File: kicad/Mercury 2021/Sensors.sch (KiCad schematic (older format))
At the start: 10 parts

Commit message: Updated new board
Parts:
- added J16: Conn_01x16_Female, symbol Connector:Conn_01x16_Female
- added J17: Conn_01x06_Female, symbol Connector:Conn_01x06_Female
- added J18: Conn_01x02_Female, symbol Connector:Conn_01x02_Female
- added J19: Conn_01x09_Female, symbol Connector:Conn_01x09_Female
- added J20: Conn_01x08_Female, symbol Connector:Conn_01x08_Female
- added J21: Conn_01x04_Female, symbol Connector:Conn_01x04_Female
- U2, U3, U4, U5, U6, U7, U8, U9: renamed from U?; footprint Sensor_Distance:ST_VL53L1x -> Connector_PinHeader_2.54mm:PinHeader_1x06_P2.54mm_Vertical
- gave numbers to parts that had none: 2
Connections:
- net MP_A0: now reaches U10.1 (A0)
- net MP_A0: now also J21.1 (Pin_1)
- net MP_GND: now reaches U10.12 (GND)
- net MP_A1: now reaches U10.2 (A1)
- net MP_A1: now also J21.2 (Pin_2)
- net MP_A2: now reaches U10.21 (A2)
- net MP_A2: now also J21.3 (Pin_3)
- net MP_+5V: now reaches U10.24 (VCC)
- net MP_Reset: now reaches U10.3 (~RESET)
- net MP_Reset: now also J21.4 (Pin_4)
- net Arduino_Tx: now reaches A1.1 (TX1)
- net Arduino_Tx: now also J18.2 (Pin_2)
- net Arduino_D7: now reaches A1.10 (D7)
- net Arduino_D7: now also J19.4 (Pin_4)
- net Arduino_D8: now reaches A1.11 (D8)
- net Arduino_D8: now also J19.3 (Pin_3)
- net Arduino_D9: now reaches A1.12 (D9)
- net Arduino_D9: now also J19.2 (Pin_2)
- net Arduino_D10: now reaches A1.13 (D10)
- net Arduino_D10: now also J19.1 (Pin_1)
- net Arduino_3v3: now reaches A1.17 (3V3)
- net Arduino_3v3: now also J17.4 (Pin_4)
- net Arduino_AREF: now reaches A1.18 (AREF)
- net Arduino_AREF: now also J17.1 (Pin_1)
- net Arduino_A0: now reaches A1.19 (A0)
- net Arduino_A0: now also J20.1 (Pin_1)
- net Arduino_Rx: now reaches A1.2 (RX1)
- net Arduino_Rx: now also J18.1 (Pin_1)
- net Arduino_A1: now reaches A1.20 (A1)
- net Arduino_A1: now also J20.2 (Pin_2)
- net Arduino_A2: now reaches A1.21 (A2)
- net Arduino_A2: now also J20.3 (Pin_3)
- net Arduino_A3: now reaches A1.22 (A3)
- net Arduino_A3: now also J20.4 (Pin_4)
- net Arduino_A7: now reaches A1.25 (A6)
- net Arduino_A7: now also J20.7 (Pin_7)
- net Arduino_A8: now reaches A1.26 (A7)
- net Arduino_A8: now also J20.8 (Pin_8)
- net Arduino_5v: now reaches A1.27 (+5V)
- net Arduino_5v: now also J17.5 (Pin_5)
- net Arduino_GND: now reaches A1.29 (GND), A1.4 (GND)
- net Arduino_GND: now also J17.3 (Pin_3)
- net Arduino_Reset: now reaches A1.3 (~RESET)
- net Arduino_Reset: now also J17.6 (Pin_6)
- net Arduino_VIN: now reaches A1.30 (VIN)
- net Arduino_VIN: now also J17.2 (Pin_2)
- net Arduino_D2: now reaches A1.5 (D2)
- net Arduino_D2: now also J19.9 (Pin_9)
- net Arduino_D3: now reaches A1.6 (D3)
- net Arduino_D3: now also J19.8 (Pin_8)
- net Arduino_D4: now reaches A1.7 (D4)
- net Arduino_D4: now also J19.7 (Pin_7)
- net Arduino_D5: now reaches A1.8 (D5)
- net Arduino_D5: now also J19.6 (Pin_6)
- net Arduino_D6: now reaches A1.9 (D6)
- net Arduino_D6: now also J19.5 (Pin_5)
- net VDD0: now reaches U3.11 (AVDD)
- net GND0: now reaches U3.12 (GND), U3.3 (GND), U3.4 (GND), U3.6 (GND)
- net Sense0_XShut: now reaches U3.5 (XSHUT)
- net Sense0_XShut: now also J16.15 (Pin_15)
- net Sense0_GPIO: now reaches U3.7 (GPIO1)
- net Sense0_GPIO: now also J16.16 (Pin_16)
- net VDD1: now reaches U5.11 (AVDD)
- net GND1: now reaches U5.12 (GND), U5.3 (GND), U5.4 (GND), U5.6 (GND)
- net Sense1_XShut: now reaches U5.5 (XSHUT)
- net Sense1_XShut: now also J16.13 (Pin_13)
- net Sense1_GPIO: now reaches U5.7 (GPIO1)
- net Sense1_GPIO: now also J16.14 (Pin_14)
- net VDD2: now reaches U7.11 (AVDD)
- net GND2: now reaches U7.12 (GND), U7.3 (GND), U7.4 (GND), U7.6 (GND)
- net Sense2_XShut: now reaches U7.5 (XSHUT)
- net Sense2_XShut: now also J16.11 (Pin_11)
- net Sense2_GPIO: now reaches U7.7 (GPIO1)
- net Sense2_GPIO: now also J16.12 (Pin_12)
- net VDD3: now reaches U9.11 (AVDD)
- net GND3: now reaches U9.12 (GND), U9.3 (GND), U9.4 (GND), U9.6 (GND)
- net Sense3_XShut: now reaches U9.5 (XSHUT)
- net Sense3_XShut: now also J16.9 (Pin_9)
- net Sense3_GPIO: now reaches U9.7 (GPIO1)
- net Sense3_GPIO: now also J16.10 (Pin_10)
- net VDD8: now reaches U8.11 (AVDD)
- net GND8: now reaches U8.12 (GND), U8.3 (GND), U8.4 (GND), U8.6 (GND)
- net Sense7_XShut: now reaches U8.5 (XSHUT)
- net Sense7_XShut: now also J16.1 (Pin_1)
- net Sense7_GPIO: now reaches U8.7 (GPIO1)
- net Sense7_GPIO: now also J16.2 (Pin_2)
- net VDD7: now reaches U6.11 (AVDD)
- net GND7: now reaches U6.12 (GND), U6.3 (GND), U6.4 (GND), U6.6 (GND)
- net Sense6_XShut: now reaches U6.5 (XSHUT)
- net Sense6_XShut: now also J16.3 (Pin_3)
- net Sense6_GPIO: now reaches U6.7 (GPIO1)
- net Sense6_GPIO: now also J16.4 (Pin_4)
- net VDD6: now reaches U4.11 (AVDD)
- net GND6: now reaches U4.12 (GND), U4.3 (GND), U4.4 (GND), U4.6 (GND)
- net Sense5_XShut: now reaches U4.5 (XSHUT)
- net Sense5_XShut: now also J16.5 (Pin_5)
- net Sense5_GPIO: now reaches U4.7 (GPIO1)
- net Sense5_GPIO: now also J16.6 (Pin_6)
- net VDD5: now reaches U2.11 (AVDD)
- net GND5: now reaches U2.12 (GND), U2.3 (GND), U2.4 (GND), U2.6 (GND)
- net Sense4_XShut: now reaches U2.5 (XSHUT)
- net Sense4_XShut: now also J16.7 (Pin_7)
- net Sense4_GPIO: now reaches U2.7 (GPIO1)
- net Sense4_GPIO: now also J16.8 (Pin_8)
- new net NC: J20.5 (Pin_5), J20.6 (Pin_6)
- no-connect marks 30 -> 22
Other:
- moved on the sheet: A1

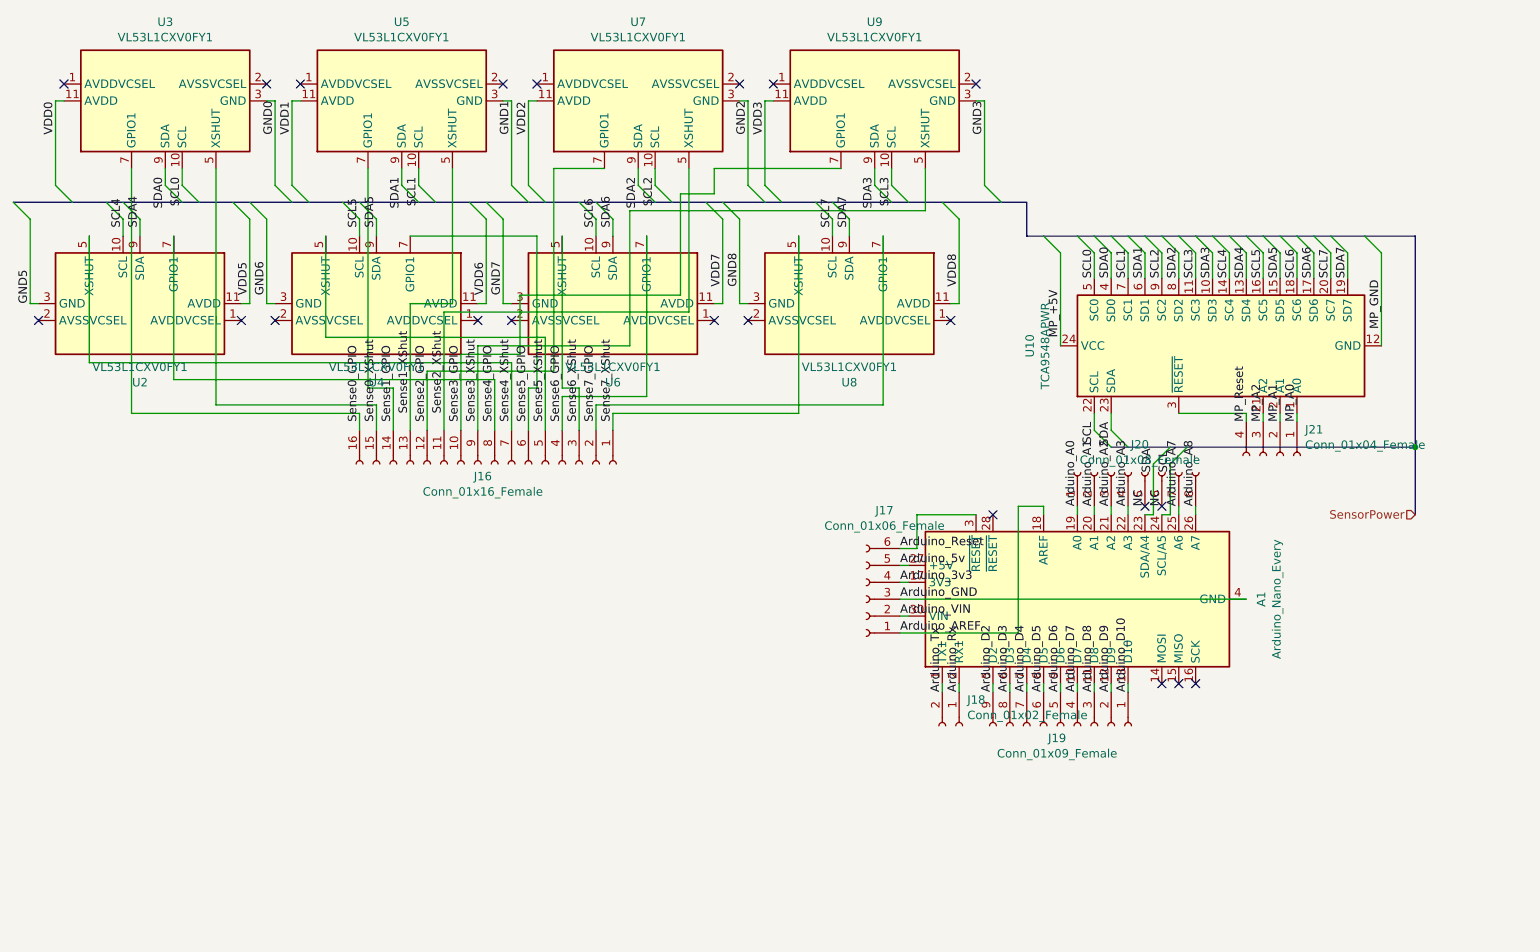
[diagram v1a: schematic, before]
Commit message: Updated the new PCB (lots of notes)
- added net
- changed symbols
- added footprints
- added ability to put the pi -> arduino cable through the board
- fixed global labels
- named connectors
- started adding things to title block

Notes:
- footprints for some parts were chosen at random, connectors need to be chosen on digikey
-- connectors for ribbon cables
-- USB connectors
-- screw terminals
- for these, the footprints may be wrong, so we need to make sure the connectors for them are spaced right
-- arduino
-- servo controller
-- PWM controller
- Board is unorganized, cluttered, and unusable, needs to be managed. considerations:
-- Pins carrying power and data should be separated by distance or GND
-- able to access connectors (not blocked by other things)
- Finish adding things to the title blocks and the PCB silkscreen
-- names or members
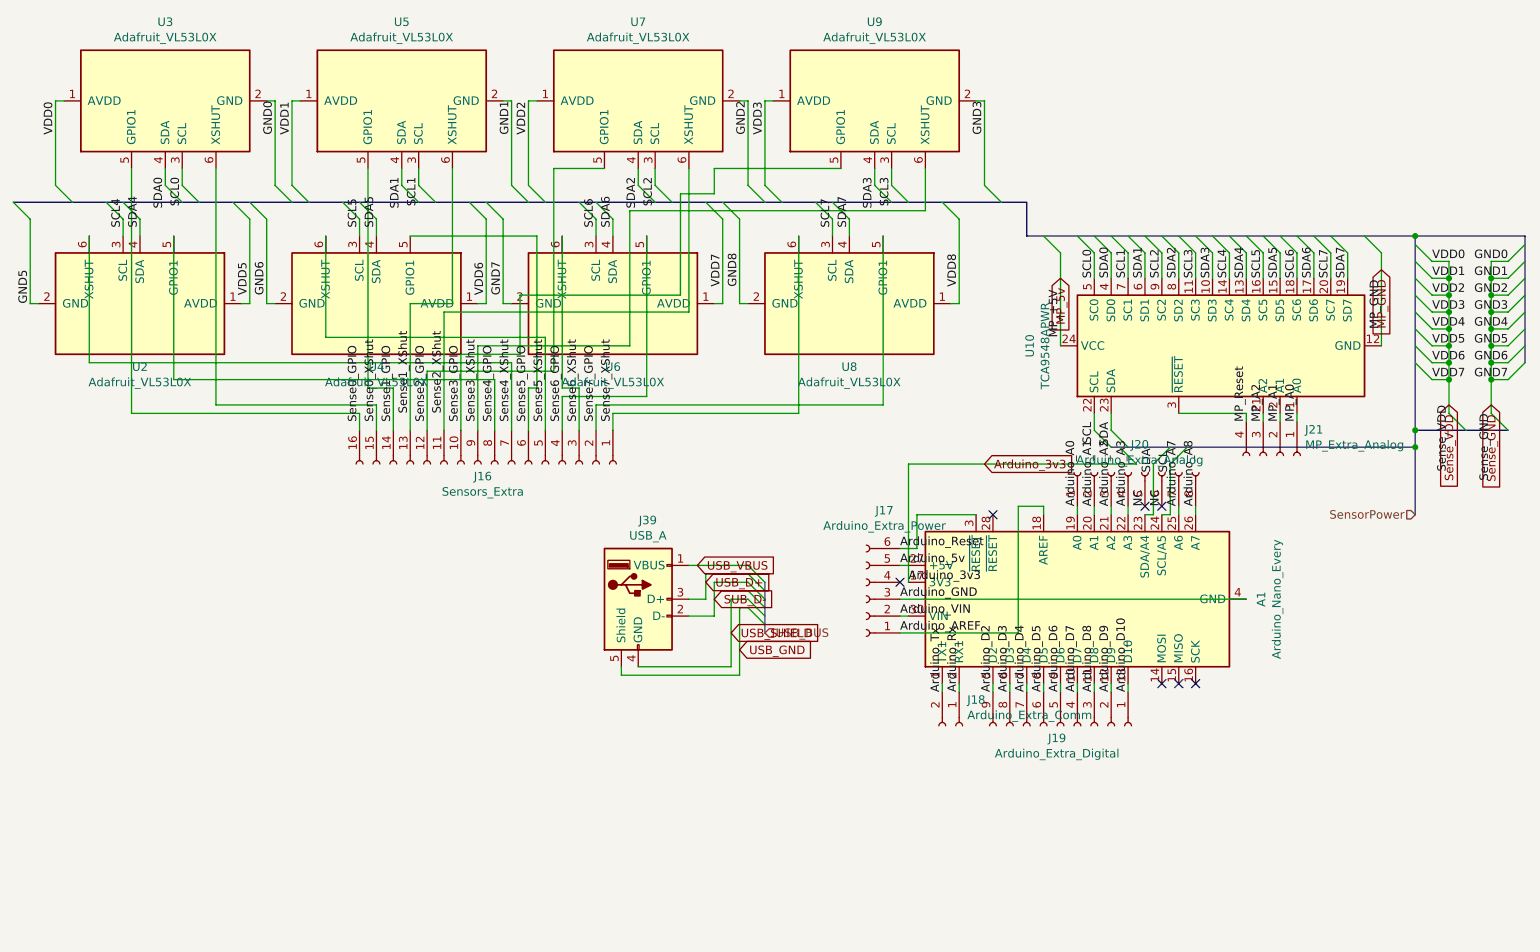
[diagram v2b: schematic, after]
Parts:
- removed U2, U3, U4, U5, U6, U7, U8, U9: VL53L1CXV0FY1, Connector_PinHeader_2.54mm:PinHeader_1x06_P2.54mm_Vertical, symbol Sensor_Distance:VL53L1CXV0FY1
- added J39: USB_A, Connector_USB:USB_A_Molex_105057_Vertical, symbol Connector:USB_A
- added U2, U3, U4, U5, U6, U7, U8, U9: Adafruit_VL53L0X, Mercury 2021:VL53L0X, symbol Sensor_Distance:Adafruit_VL53L0X
- A1: footprint Module:Arduino_Nano -> Module:Arduino_Nano_WithMountingHoles
- J16: value Conn_01x16_Female -> Sensors_Extra; footprint (none) -> Connector_PinSocket_2.54mm:PinSocket_1x16_P2.54mm_Vertical
- J17: value Conn_01x06_Female -> Arduino_Extra_Power; footprint (none) -> Connector_PinSocket_2.54mm:PinSocket_1x06_P2.54mm_Vertical
- J18: value Conn_01x02_Female -> Arduino_Extra_Comm; footprint (none) -> Connector_PinSocket_2.54mm:PinSocket_1x02_P2.54mm_Vertical
- J19: value Conn_01x09_Female -> Arduino_Extra_Digital; footprint (none) -> Connector_PinSocket_2.54mm:PinSocket_1x09_P2.54mm_Vertical
- J20: value Conn_01x08_Female -> Arduino_Extra_Analog; footprint (none) -> Connector_PinSocket_2.54mm:PinSocket_1x08_P2.54mm_Vertical
- J21: value Conn_01x04_Female -> MP_Extra_Analog; footprint (none) -> Connector_PinSocket_2.54mm:PinSocket_1x04_P2.54mm_Vertical
- U10: footprint Package_SO:TSSOP-24_4.4x7.8mm_P0.65mm -> Mercury 2021:TCA9548
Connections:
- net Arduino_3v3: no longer J17.4 (Pin_4)
- net GND8: now also U8.2 (GND)
- net SCL0: now also U3.3 (SCL)
- net SCL1: now also U5.3 (SCL)
- net SCL2: now also U7.3 (SCL)
- net SCL3: now also U9.3 (SCL)
- net SCL4: now also U2.3 (SCL)
- net SCL5: now also U4.3 (SCL)
- net SCL6: now also U6.3 (SCL)
- net SCL7: now also U8.3 (SCL)
- net SDA0: now also U3.4 (SDA)
- net SDA1: now also U5.4 (SDA)
- net SDA2: now also U7.4 (SDA)
- net SDA3: now also U9.4 (SDA)
- net SDA4: now also U2.4 (SDA)
- net SDA5: now also U4.4 (SDA)
- net SDA6: now also U6.4 (SDA)
- net SDA7: now also U8.4 (SDA)
- net Sense0_GPIO: now also U3.5 (GPIO1)
- net Sense0_XShut: now also U3.6 (XSHUT)
- net Sense1_GPIO: now also U5.5 (GPIO1)
- net Sense1_XShut: now also U5.6 (XSHUT)
- net Sense2_GPIO: now also U7.5 (GPIO1)
- net Sense2_XShut: now also U7.6 (XSHUT)
- net Sense3_GPIO: now also U9.5 (GPIO1)
- net Sense3_XShut: now also U9.6 (XSHUT)
- net Sense4_GPIO: now also U2.5 (GPIO1)
- net Sense4_XShut: now also U2.6 (XSHUT)
- net Sense5_GPIO: now also U4.5 (GPIO1)
- net Sense5_XShut: now also U4.6 (XSHUT)
- net Sense6_GPIO: now also U6.5 (GPIO1)
- net Sense6_XShut: now also U6.6 (XSHUT)
- net Sense7_GPIO: now also U8.5 (GPIO1)
- net Sense7_XShut: now also U8.6 (XSHUT)
- net VDD8: now also U8.1 (AVDD)
- net MP_+5V renamed MP_5v
- new net SUB_D-: J39.2 (D-)
- new net Sense_GND: U2.2 (GND), U3.2 (GND), U4.2 (GND), U5.2 (GND), U6.2 (GND), U7.2 (GND), U9.2 (GND)
- new net Sense_VDD: U2.1 (AVDD), U3.1 (AVDD), U4.1 (AVDD), U5.1 (AVDD), U6.1 (AVDD), U7.1 (AVDD), U9.1 (AVDD)
- new net USB_D+: J39.3 (D+)
- new net USB_GND: J39.5 (Shield)
- new net USB_SHIELD: J39.4 (GND)
- new net USB_VBUS: J39.1 (VBUS)
- no-connect marks 22 -> 7

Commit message: Updated new board
- Did PCB traces
-- almost got away with just 2 copper layers, pi ruined it when there was only a bit to go. Probably possible but would take a lot of back and forth
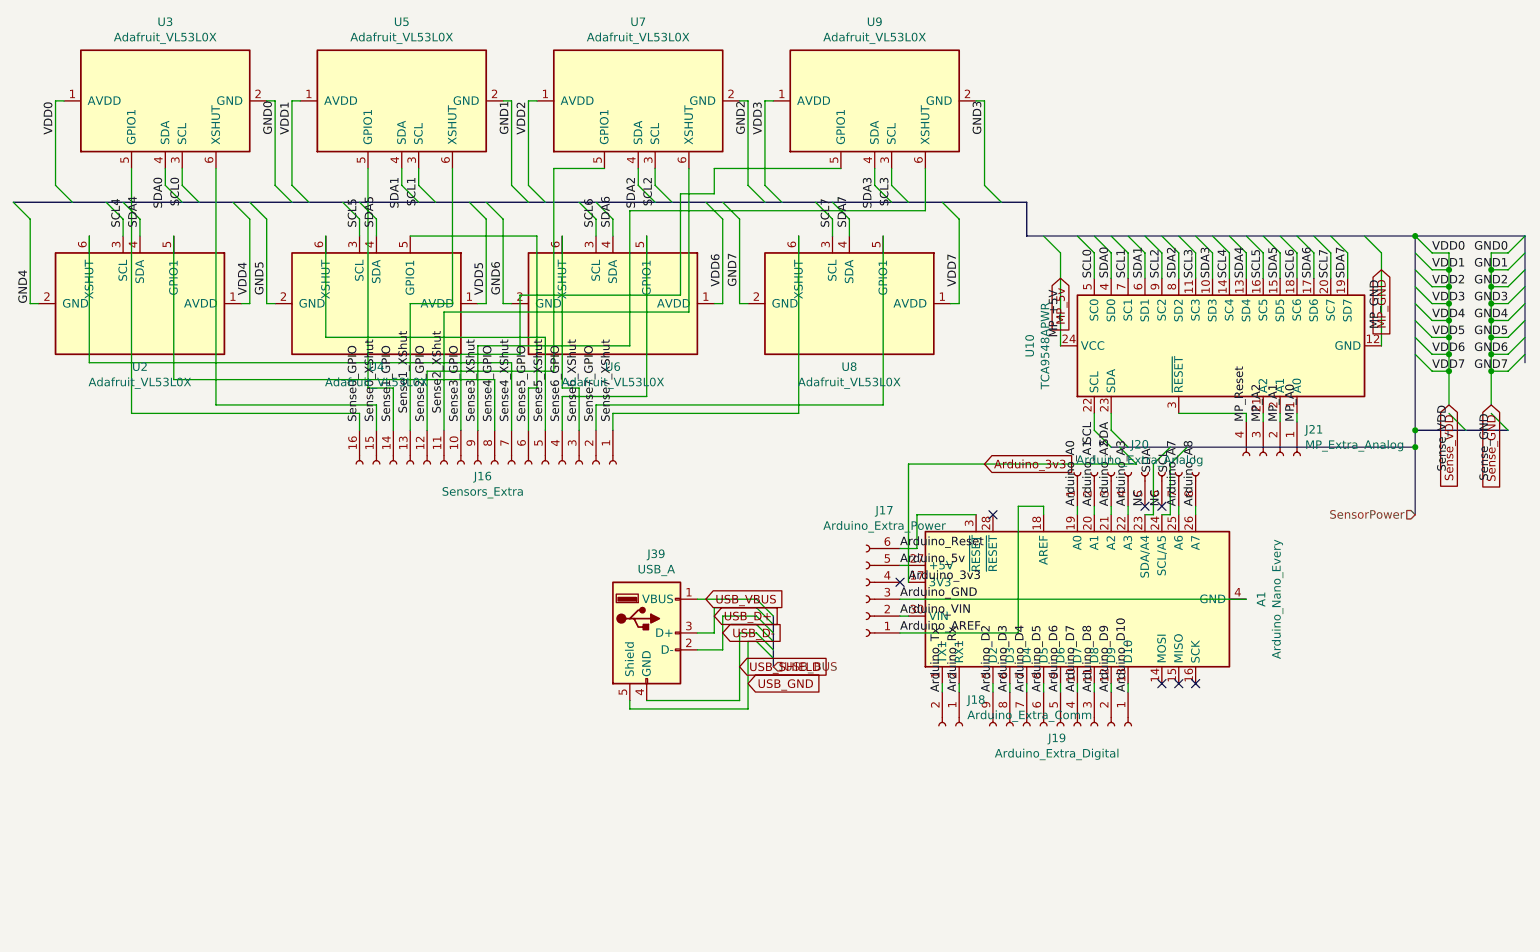
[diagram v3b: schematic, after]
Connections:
- net GND8 is gone; now on net Sense_GND: U8.2 (GND)
- net VDD8 is gone; now on net Sense_VDD: U8.1 (AVDD)
- net SUB_D- renamed USB_D-
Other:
- moved on the sheet: J39

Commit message: New New board
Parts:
- removed J39: USB_A, Connector_USB:USB_A_Molex_105057_Vertical, symbol Connector:USB_A
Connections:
- net NC renamed NCa
- net NCa: no longer J20.6 (Pin_6)
- new net NCb: J20.6 (Pin_6)
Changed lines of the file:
@@
 Arduino_A3
 Text Label 7400 3450 1    50   ~ 0
-NC
-Text Label 7500 3450 1    50   ~ 0
-NC
+NCa
 Text Label 7700 3450 1    50   ~ 0
 Arduino_A8
@@
 Text GLabel 6450 3200 2    50   Input ~ 0
 Arduino_3v3
-Text HLabel 5200 4400 2    50   Input ~ 0
-USB_BUS
-$Comp
-L Connector:USB_A J39
-U 1 1 612C23CD
-P 4450 4200
-F 0 "J39" H 4507 4667 50  0000 C CNN
-F 1 "USB_A" H 4507 4576 50  0000 C CNN
-F 2 "Connector_USB:USB_A_Molex_105057_Vertical" H 4600 4150 50  0001 C CNN
-F 3 " ~" H 4600 4150 50  0001 C CNN
-	1    4450 4200
-	1    0    0    -1
-$EndComp
-Wire Wire Line
-	4750 4200 4850 4200
-Wire Wire Line
-	4850 4200 4850 4050
-Wire Wire Line
-	4750 4300 4900 4300
-Wire Wire Line
-	4900 4300 4900 4100
-Wire Wire Line
-	4450 4600 5000 4600
-Wire Wire Line
-	5000 4600 5000 4200
-Wire Wire Line
-	4350 4600 4350 4650
-Wire Wire Line
-	4350 4650 5050 4650
-Wire Wire Line
-	5050 4250 5100 4250
-Wire Wire Line
-	5000 4200 5100 4200
-Wire Wire Line
-	4950 4150 5100 4150
-Wire Wire Line
-	4900 4100 5100 4100
-Wire Wire Line
-	4850 4050 5100 4050
-Entry Wire Line
-	5100 4000 5200 4100
-Entry Wire Line
-	5100 4050 5200 4150
-Entry Wire Line
-	5100 4100 5200 4200
-Entry Wire Line
-	5100 4150 5200 4250
-Entry Wire Line
-	5100 4200 5200 4300
-Entry Wire Line
-	5100 4250 5200 4350
-Text GLabel 4800 4000 2    50   Input ~ 0
-USB_VBUS
-Text GLabel 4850 4100 2    50   Input ~ 0
-USB_D+
-Text GLabel 4900 4200 2    50   Input ~ 0
-USB_D-
-Text GLabel 5000 4400 2    50   Input ~ 0
-USB_SHIELD
-Text GLabel 5050 4500 2    50   Input ~ 0
-USB_GND
 Wire Wire Line
 	1900 2850 2850 2850
@@
 Wire Wire Line
 	5950 4000 8000 4000
-Wire Wire Line
-	5100 4000 4750 4000
-Wire Wire Line
-	5050 4250 5050 4650
-Wire Bus Line
-	5200 4100 5200 4400
 Wire Bus Line
 	9000 3000 9550 3000
 Wire Bus Line
+	7200 3100 9000 3100
+Wire Bus Line
 	9650 1850 9650 2600
 Wire Bus Line
 	9000 1850 9000 3000
 Wire Bus Line
-	7200 3100 9000 3100
+	6700 1850 9000 1850
 Wire Bus Line
 	700  1650 6700 1650
-Wire Bus Line
-	6700 1850 9000 1850
+Text Label 7500 3450 1    50   ~ 0
+NCb
 $EndSCHEMATC

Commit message: Updated PCB
Updated Labels & arduino now powered off of board.
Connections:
- net Arduino_GND renamed GND_Rail
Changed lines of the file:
@@
 Text Label 6300 2150 1    50   ~ 0
 VDD7
-Wire Bus Line
-	9000 3100 9000 3500
 Connection ~ 9000 3100
 Text HLabel 9000 3500 0    50   Input ~ 0
@@
 Wire Wire Line
 	6000 3800 5950 3800
-Wire Wire Line
-	5950 4100 6000 4100
 Text Label 5950 4100 0    50   ~ 0
 Arduino_VIN
@@
 	5950 4200 6650 4200
 Wire Wire Line
-	5950 4000 8000 4000
+	5950 4000 7700 4000
 Text Label 7500 3450 1    50   ~ 0
 NCb
+Wire Wire Line
+	6550 4100 6550 3400
+Wire Wire Line
+	6550 3400 8850 3400
+Wire Wire Line
+	5950 4100 6000 4100
+Connection ~ 6000 4100
+Wire Wire Line
+	6000 4100 6550 4100
+Entry Wire Line
+	8900 3300 9000 3400
+Wire Wire Line
+	8900 3300 8850 3300
+Wire Wire Line
+	8850 3300 8850 3400
+Text GLabel 8900 3300 0    50   Input ~ 0
+Arduino_VIN
+Entry Wire Line
+	9000 3300 9100 3400
+Wire Wire Line
+	9100 3400 9100 3900
+Wire Wire Line
+	9100 3900 7700 3900
+Wire Wire Line
+	7700 3900 7700 4000
 Wire Bus Line
 	9000 3000 9550 3000
 Wire Bus Line
+	9000 3100 9000 3500
+Wire Bus Line
 	7200 3100 9000 3100
 Wire Bus Line
@@
 Wire Bus Line
 	700  1650 6700 1650
+Connection ~ 7700 4000
+Wire Wire Line
+	7700 4000 8000 4000
+Text GLabel 9100 3400 0    50   Input ~ 0
+GND_Rail
 $EndSCHEMATC
